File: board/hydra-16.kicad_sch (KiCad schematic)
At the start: 33 parts, among them J1 Conn_01x32, J2 Conn_01x24, J3 DE9_Plug, U3 AT28C64B, U4 W65C02S, U5 65C22, U6 65C51, U7 MAX232, U8 Task RAM, U9 74F138

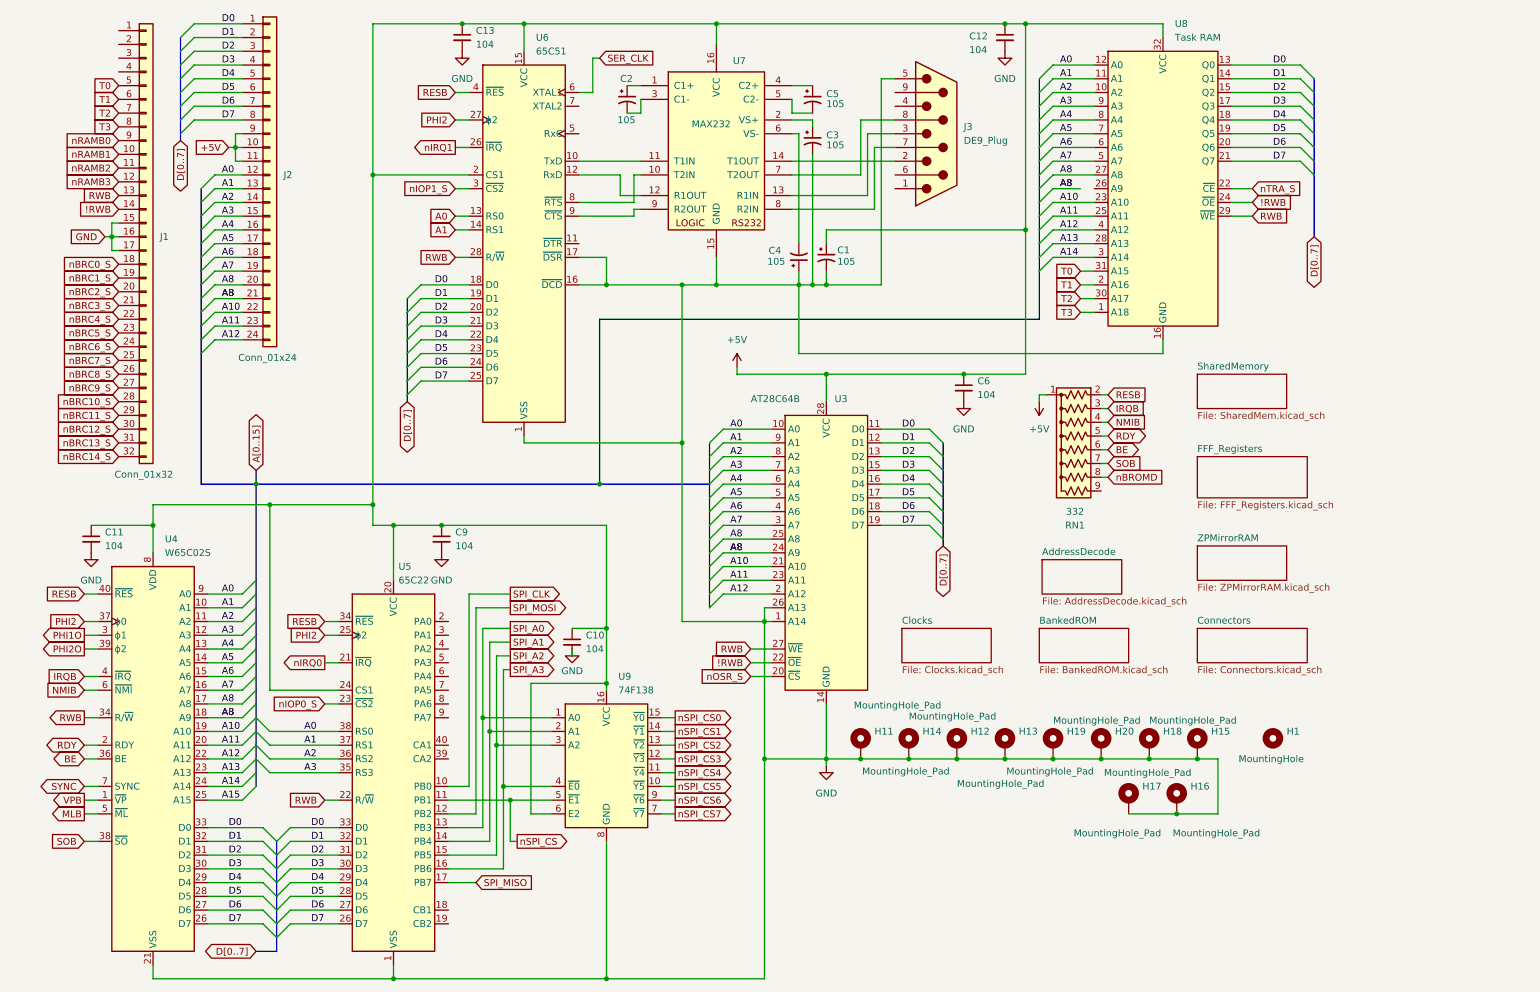
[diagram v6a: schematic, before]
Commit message: Added VIA port A header and voltage protection diode package socket. Updated logic.
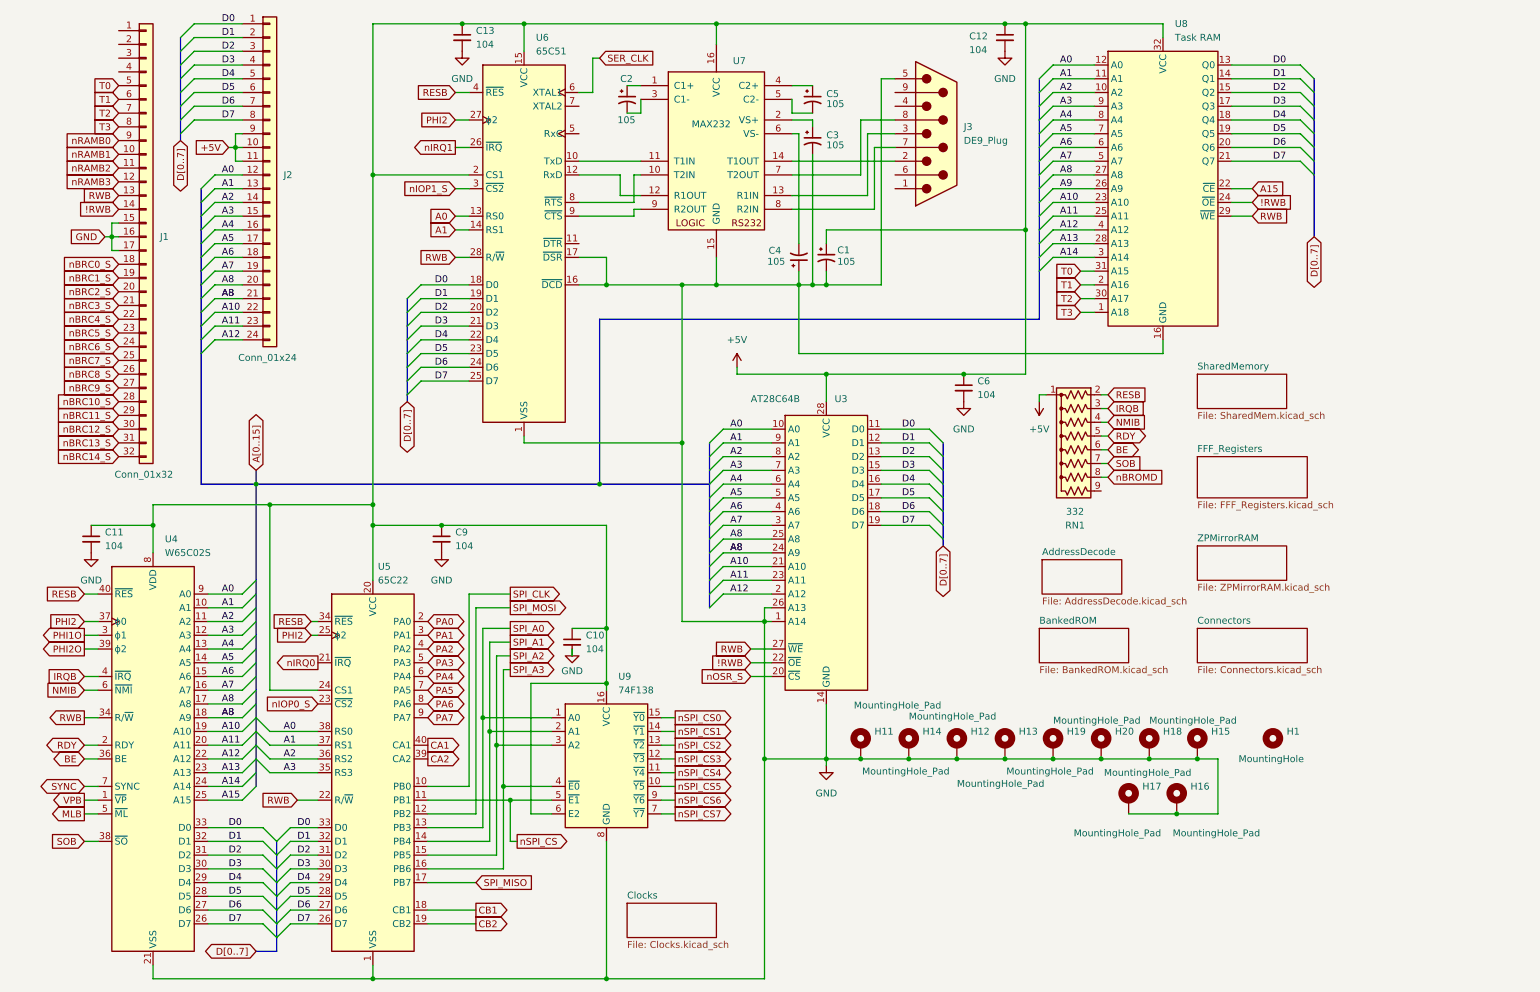
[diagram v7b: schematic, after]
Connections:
- net nTRA_S is gone; now on net A15: U8.22 (~{CE})
- net CB1: now reaches U5.18 (CB1)
- net CB2: now reaches U5.19 (CB2)
- net PA0: now reaches U5.2 (PA0)
- net PA1: now reaches U5.3 (PA1)
- net CA2: now reaches U5.39 (CA2)
- net PA2: now reaches U5.4 (PA2)
- net CA1: now reaches U5.40 (CA1)
- net PA3: now reaches U5.5 (PA3)
- net PA4: now reaches U5.6 (PA4)
- net PA5: now reaches U5.7 (PA5)
- net PA6: now reaches U5.8 (PA6)
- net PA7: now reaches U5.9 (PA7)
- net A9: now reaches U8.26 (A9)
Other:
- moved on the sheet: U5

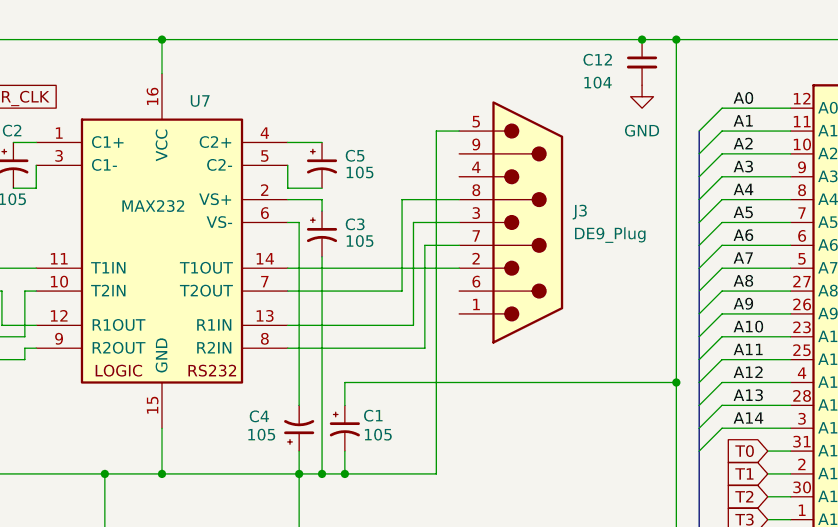
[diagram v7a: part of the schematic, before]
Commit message: Initial production breakout card and main PCB versions
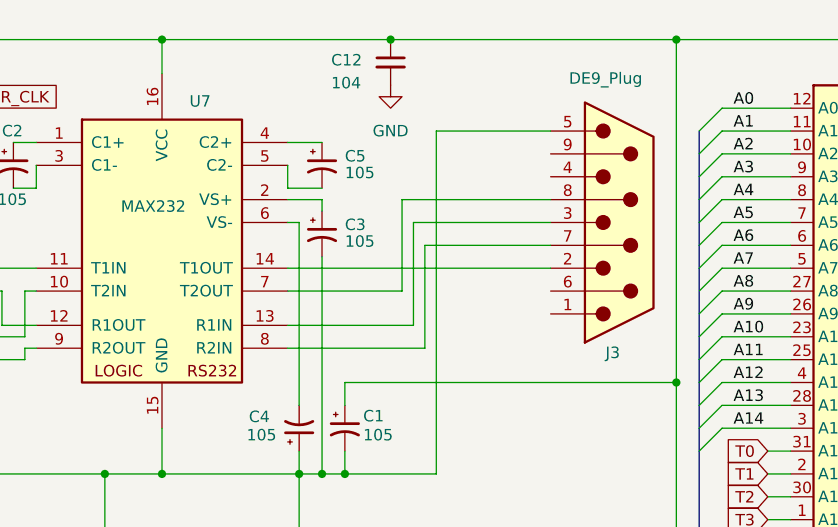
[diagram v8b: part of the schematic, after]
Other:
- moved on the sheet: C12, J3
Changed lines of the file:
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@@
 		(title "CPU, VIA, ACIA, O/S ROM, Task RAM and Banked RAM Connector")
 		(date "2024-10-09")
-		(rev "0.1A")
+		(rev "0.3B")
 		(company "Data Tuning")
 		(comment 1 "Hydra 16")
@@
 	)
 	(junction
-		(at 196.85 16.51)
+		(at 168.91 16.51)
 		(diameter 0)
 		(color 0 0 0 0)
@@
 	(wire
 		(pts
-			(xy 176.53 26.67) (xy 173.99 26.67)
+			(xy 186.69 26.67) (xy 173.99 26.67)
 		)
 		(stroke
@@
 	(wire
 		(pts
-			(xy 176.53 39.37) (xy 172.72 39.37)
+			(xy 186.69 39.37) (xy 172.72 39.37)
 		)
 		(stroke
@@
 	(wire
 		(pts
-			(xy 176.53 36.83) (xy 171.45 36.83)
+			(xy 143.51 16.51) (xy 168.91 16.51)
+		)
+		(stroke
+			(width 0)
+			(type default)
+		)
+	)
+	(wire
+		(pts
+			(xy 186.69 36.83) (xy 171.45 36.83)
 		)
 		(stroke
@@
 	(wire
 		(pts
-			(xy 196.85 16.51) (xy 200.66 16.51)
+			(xy 168.91 16.51) (xy 200.66 16.51)
 		)
 		(stroke
@@
 	(wire
 		(pts
-			(xy 143.51 16.51) (xy 196.85 16.51)
-		)
-		(stroke
-			(width 0)
-			(type default)
-		)
-	)
-	(wire
-		(pts
 			(xy 123.19 128.27) (xy 123.19 109.22)
 		)
@@
 	(wire
 		(pts
-			(xy 176.53 34.29) (xy 170.18 34.29)
+			(xy 186.69 34.29) (xy 170.18 34.29)
 		)
 		(stroke
@@
 	(wire
 		(pts
-			(xy 157.48 41.91) (xy 176.53 41.91)
-		)
-		(stroke
-			(width 0)
-			(type default)
-		)
-	)
-	(wire
-		(pts
 			(xy 215.9 87.63) (xy 214.63 87.63)
 		)
@@
 	(wire
 		(pts
+			(xy 157.48 41.91) (xy 186.69 41.91)
+		)
+		(stroke
+			(width 0)
+			(type default)
+		)
+	)
+	(wire
+		(pts
 			(xy 39.37 105.41) (xy 60.96 105.41)
 		)
@@
 	(symbol
 		(lib_id "power:GND")
-		(at 196.85 21.59 0)
+		(at 168.91 21.59 0)
 		(unit 1)
 		(exclude_from_sim no)
@@
 		(fields_autoplaced yes)
 		(property "Reference" "#PWR09"
-			(at 196.85 27.94 0)
+			(at 168.91 27.94 0)
 			(effects
 				(font
@@
 		)
 		(property "Value" "GND"
-			(at 196.85 26.67 0)
+			(at 168.91 26.67 0)
 			(effects
 				(font
@@
 		)
 		(property "Footprint" ""
-			(at 196.85 21.59 0)
+			(at 168.91 21.59 0)
 			(effects
 				(font
@@
 		)
 		(property "Datasheet" ""
-			(at 196.85 21.59 0)
+			(at 168.91 21.59 0)
 			(effects
 				(font
@@
 		)
 		(property "Description" "Power symbol creates a global label with name \"GND\" , ground"
-			(at 196.85 21.59 0)
+			(at 168.91 21.59 0)
 			(effects
 				(font
@@
 	(symbol
 		(lib_id "Connector:DE9_Plug")
-		(at 184.15 36.83 0)
+		(at 194.31 36.83 0)
 		(unit 1)
 		(exclude_from_sim no)
@@
 		(on_board yes)
 		(dnp no)
-		(fields_autoplaced yes)
 		(property "Reference" "J3"
-			(at 189.23 35.5599 0)
+			(at 192.786 51.308 0)
 			(effects
 				(font
@@
 		)
 		(property "Value" "DE9_Plug"
-			(at 189.23 38.0999 0)
+			(at 188.722 20.828 0)
 			(effects
 				(font
@@
 		)
 		(property "Footprint" "Connector_Dsub:DSUB-9_Male_Horizontal_P2.77x2.54mm_EdgePinOffset9.40mm"
-			(at 184.15 36.83 0)
+			(at 194.31 36.83 0)
 			(effects
 				(font
@@
 		)
 		(property "Datasheet" "~"
-			(at 184.15 36.83 0)
+			(at 194.31 36.83 0)
 			(effects
 				(font
@@
 		)
 		(property "Description" "9-pin male plug pin D-SUB connector"
-			(at 184.15 36.83 0)
+			(at 194.31 36.83 0)
 			(effects
 				(font
@@
 	(symbol
 		(lib_id "Device:C_Small")
-		(at 196.85 19.05 0)
+		(at 168.91 19.05 0)
 		(unit 1)
 		(exclude_from_sim no)
@@
 		(dnp no)
 		(property "Reference" "C12"
-			(at 190.246 18.796 0)
+			(at 162.306 18.796 0)
 			(effects
 				(font
@@
 		)
 		(property "Value" "104"
-			(at 190.246 21.336 0)
+			(at 162.306 21.336 0)
 			(effects
 				(font
@@
 		)
 		(property "Footprint" "Capacitor_THT:C_Disc_D5.0mm_W2.5mm_P5.00mm"
-			(at 196.85 19.05 0)
+			(at 168.91 19.05 0)
 			(effects
 				(font
@@
 		)
 		(property "Datasheet" "~"
-			(at 196.85 19.05 0)
+			(at 168.91 19.05 0)
 			(effects
 				(font
@@
 		)
 		(property "Description" "Unpolarized capacitor, small symbol"
-			(at 196.85 19.05 0)
+			(at 168.91 19.05 0)
 			(effects
 				(font
